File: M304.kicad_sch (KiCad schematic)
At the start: 89 parts, among them J1 LCD 2004, J2 Relay OUT, J3 iM920, J4 GPS, J5 Conn_01x02, P1 Digital, P10 CONN_01X01, P11 CONN_01X01, P12 CONN_01X01, P13 CONN_01X01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

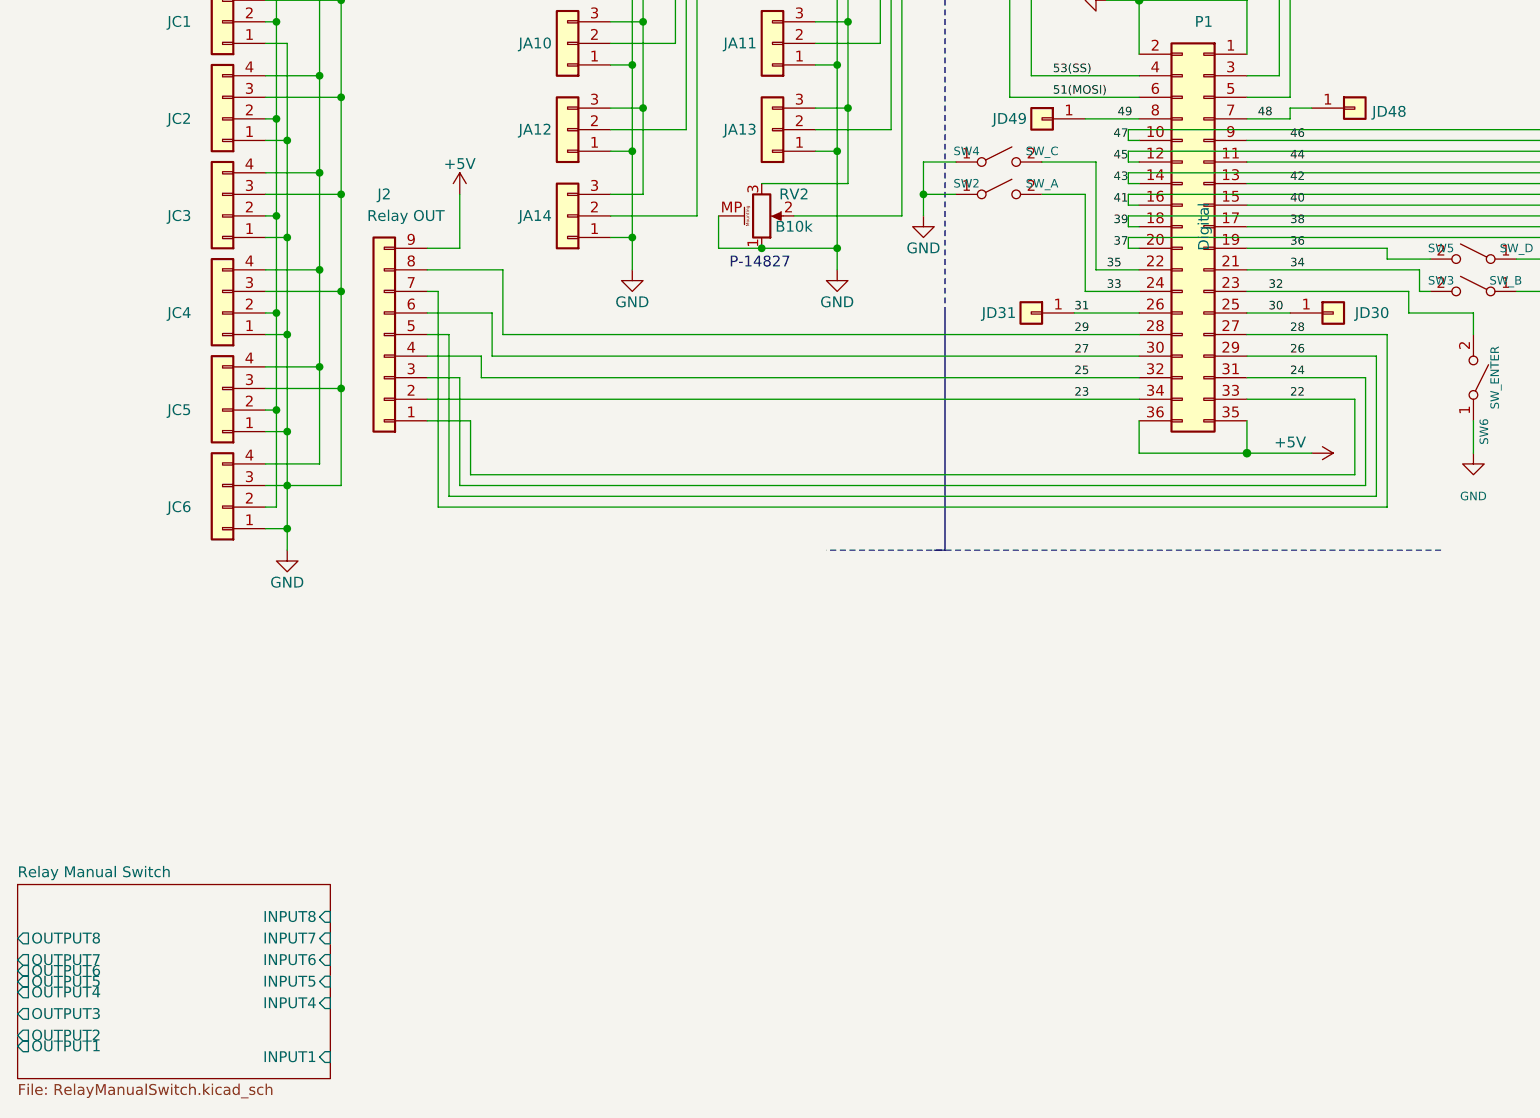
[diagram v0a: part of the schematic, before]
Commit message: RelayManualSwitch回路充実
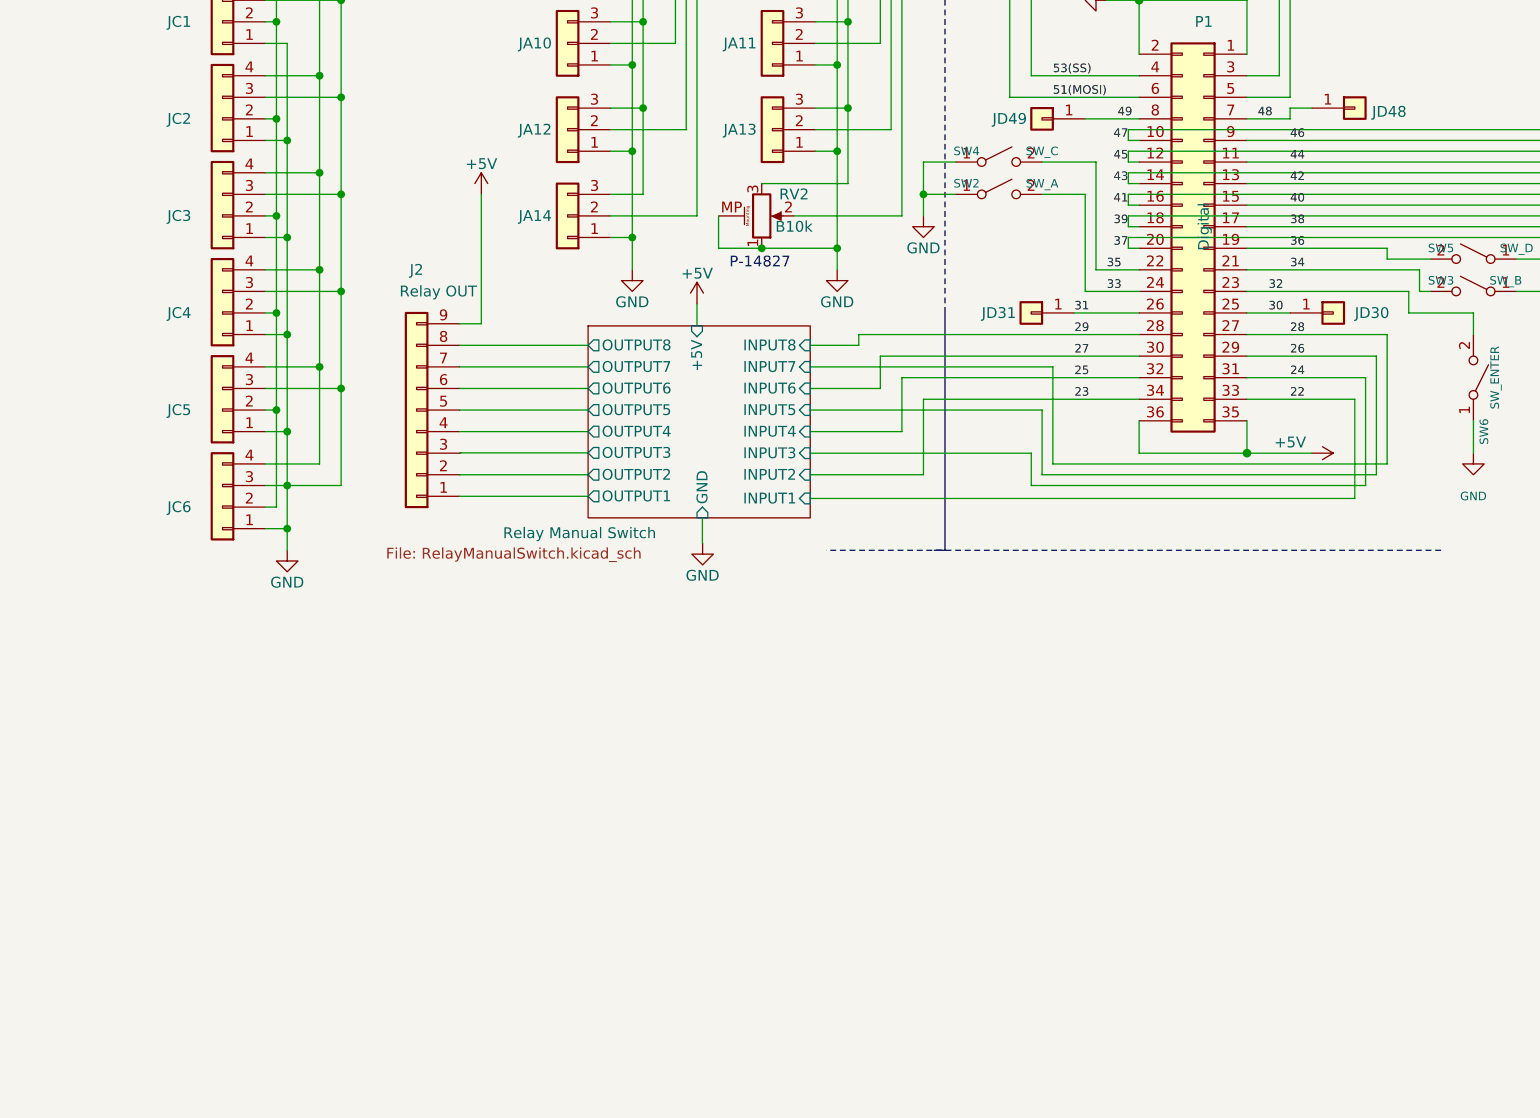
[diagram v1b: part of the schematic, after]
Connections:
- net 22: no longer J2.1 (Pin_1)
- net 23: no longer J2.2 (Pin_2)
- net 24: no longer J2.3 (Pin_3)
- net 25: no longer J2.4 (Pin_4)
- net 26: no longer J2.5 (Pin_5)
- net 27: no longer J2.6 (Pin_6)
- net 28: no longer J2.7 (Pin_7)
- net 29: no longer J2.8 (Pin_8)
- net Relay Manual Switch/OUTPUT1: now also J2.1 (Pin_1)
- net Relay Manual Switch/OUTPUT2: now also J2.2 (Pin_2)
- net Relay Manual Switch/OUTPUT3: now also J2.3 (Pin_3)
- net Relay Manual Switch/OUTPUT4: now also J2.4 (Pin_4)
- net Relay Manual Switch/OUTPUT5: now also J2.5 (Pin_5)
- net Relay Manual Switch/OUTPUT6: now also J2.6 (Pin_6)
- net Relay Manual Switch/OUTPUT7: now also J2.7 (Pin_7)
- net Relay Manual Switch/OUTPUT8: now also J2.8 (Pin_8)
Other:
- sheet Relay Manual Switch ports: added +5V, GND, INPUT2, INPUT3; removed none
- moved on the sheet: J2

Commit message: Mode STAT monitoring
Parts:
- removed JD31: Conn_01x01, Connector_Pin:Pin_D0.9mm_L10.0mm_W2.4mm_FlatFork, symbol Connector_Generic:Conn_01x01
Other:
- sheet Relay Manual Switch ports: added STAT; removed none
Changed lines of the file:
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@@
     (stroke (width 0) (type solid) (color 0 0 0 0))
   )
+  (wire (pts (xy 83.82 163.83) (xy 133.35 163.83))
+    (stroke (width 0) (type default) (color 0 0 0 0))
+  )
   (wire (pts (xy 252.73 30.48) (xy 255.27 30.48))
     (stroke (width 0) (type default) (color 0 0 0 0))
@@
     (stroke (width 0) (type default) (color 0 0 0 0))
   )
-  (wire (pts (xy 133.35 163.83) (xy 125.73 163.83))
-    (stroke (width 0) (type solid) (color 0 0 0 0))
-  )
   (wire (pts (xy 104.14 109.22) (xy 135.89 109.22))
     (stroke (width 0) (type default) (color 0 0 0 0))
@@
     (stroke (width 0) (type default) (color 0 0 0 0))
   )
+  (wire (pts (xy 83.82 163.83) (xy 83.82 165.354))
+    (stroke (width 0) (type default) (color 0 0 0 0))
+  )
   (wire (pts (xy 271.78 17.78) (xy 269.24 17.78))
     (stroke (width 0) (type default) (color 0 0 0 0))
@@
     (pin "2")
   )
-  (symbol (lib_id "Connector_Generic:Conn_01x01") (at 120.65 163.83 0) (mirror y) (unit 1)
-    (in_bom yes) (on_board yes)
-    (property "Reference" "JD31" (id 0) (at 116.84 163.83 0))
-    (property "Value" "Conn_01x01" (id 1) (at 120.65 161.3971 0)
-      (effects (font (size 1.27 1.27)) hide)
-    )
-    (property "Footprint" "Connector_Pin:Pin_D0.9mm_L10.0mm_W2.4mm_FlatFork" (id 2) (at 120.65 163.83 0)
-      (effects (font (size 1.27 1.27)) hide)
-    )
-    (property "Datasheet" "~" (id 3) (at 120.65 163.83 0)
-      (effects (font (size 1.27 1.27)) hide)
-    )
-    (pin "1")
-  )
   (symbol (lib_id "power:GND") (at 33.02 109.22 0) (unit 1)
     (in_bom yes) (on_board yes)
@@
       (effects (font (size 1.27 1.27)) (justify left))
     )
+    (pin "STAT" input (at 83.82 165.354 90)
+      (effects (font (size 1.27 1.27)) (justify right))
+    )
   )
   (sheet_instances
@@
     )
     (path "/923cf744-f246-4b99-9093-f86e5817e7a4/74b97936-4962-4d8c-8297-ea27e9c720cb"
-      (reference "#PWR?") (unit 1) (value "GND") (footprint "")
+      (reference "#PWR0158") (unit 1) (value "GND") (footprint "")
     )
     (path "/923cf744-f246-4b99-9093-f86e5817e7a4/8eecf7a6-ba02-4b56-86c1-4b6121624f36"
-      (reference "#PWR?") (unit 1) (value "GND") (footprint "")
+      (reference "#PWR0159") (unit 1) (value "GND") (footprint "")
     )
     (path "/7629fb6d-20db-4e52-aca9-1faafbccf85c"
@@
       (reference "D2-2") (unit 1) (value "LED") (footprint "")
     )
+    (path "/923cf744-f246-4b99-9093-f86e5817e7a4/47483762-d7d0-4c20-b380-6fbcea955810"
+      (reference "D2-3") (unit 1) (value "1N4148") (footprint "Diode_THT:D_DO-35_SOD27_P7.62mm_Horizontal")
+    )
     (path "/6f005a80-49e2-4014-971a-0fdebe1c3bed"
       (reference "D3") (unit 1) (value "1N4148") (footprint "Diode_THT:D_DO-35_SOD27_P7.62mm_Horizontal")
@@
       (reference "JD30") (unit 1) (value "Conn_01x01") (footprint "Connector_Pin:Pin_D0.9mm_L10.0mm_W2.4mm_FlatFork")
     )
-    (path "/c9444dbf-6a90-407d-8c6b-f91ec54f63d1"
-      (reference "JD31") (unit 1) (value "Conn_01x01") (footprint "Connector_Pin:Pin_D0.9mm_L10.0mm_W2.4mm_FlatFork")
-    )
     (path "/b0e37c59-828f-45f4-9524-3ceeeb2c5150"
       (reference "JD48") (unit 1) (value "Conn_01x01") (footprint "Connector_Pin:Pin_D0.9mm_L10.0mm_W2.4mm_FlatFork")
@@
       (reference "R2-2") (unit 1) (value "510") (footprint "")
     )
+    (path "/923cf744-f246-4b99-9093-f86e5817e7a4/aaa27b19-2b0f-459a-a227-24bc82c9e15a"
+      (reference "R2-3") (unit 1) (value "510") (footprint "")
+    )
     (path "/2447acfb-c168-4f85-b4d3-c3630454679c"

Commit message: PCB Design start
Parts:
- BT1: footprint (none) -> Akizuki:CH74-2032LF
- J5: value Conn_01x02 -> POWER IN
- RV1: footprint (none) -> Potentiometer_THT:Potentiometer_Runtron_RM-065_Vertical
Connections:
- net +3V3: now also JA0.3 (Pin_3), JA1.3 (Pin_3), JA2.3 (Pin_3), JA3.3 (Pin_3), JA4.3 (Pin_3), JA5.3 (Pin_3), JA6.3 (Pin_3), JA7.3 (Pin_3)
- net +5V: now also C2.2; no longer C2.1, JA0.3 (Pin_3), JA1.3 (Pin_3), JA2.3 (Pin_3), JA3.3 (Pin_3), JA4.3 (Pin_3), JA5.3 (Pin_3), JA6.3 (Pin_3), JA7.3 (Pin_3)
- net GND: now also C2.1; no longer C2.2, JC1.3 (Pin_3), JC2.3 (Pin_3), JC3.3 (Pin_3), JC4.3 (Pin_3), JC5.3 (Pin_3), JC6.3 (Pin_3), P5.2 (Pin_2), R2.2, U1.5 (SDA), U2.5 (SDA)
- net at U1.1 (X1): now also Y1.1; no longer Y1.2
- net at U1.2 (X2): now also Y1.2 (1); no longer Y1.1
- new net SDA: JC1.3 (Pin_3), JC2.3 (Pin_3), JC3.3 (Pin_3), JC4.3 (Pin_3), JC5.3 (Pin_3), JC6.3 (Pin_3), P5.2 (Pin_2), R2.2, U1.5 (SDA), U2.5 (SDA)
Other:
- note added: "P-01443"
- note removed: "P-00706"
- moved on the sheet: C2, Y1

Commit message: PCB Design cont.
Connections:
- net +5V: now also R1.2; no longer R1.1
- net Reset: now also R1.1; no longer R1.2
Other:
- moved on the sheet: R1
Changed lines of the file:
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@@
     (pin "1")
   )
-  (symbol (lib_id "Device:R_US") (at 101.6 38.1 0) (unit 1)
+  (symbol (lib_id "Device:R_US") (at 101.6 38.1 180) (unit 1)
     (in_bom yes) (on_board yes) (fields_autoplaced)
     (property "Reference" "R1" (id 0) (at 103.251 37.2653 0)
-      (effects (font (size 1.27 1.27)) (justify left))
+      (effects (font (size 1.27 1.27)) (justify right))
     )
     (property "Value" "10k" (id 1) (at 103.251 39.8022 0)
-      (effects (font (size 1.27 1.27)) (justify left))
+      (effects (font (size 1.27 1.27)) (justify right))
     )
-    (property "Footprint" "Resistor_THT:R_Axial_DIN0207_L6.3mm_D2.5mm_P7.62mm_Horizontal" (id 2) (at 102.616 38.354 90)
+    (property "Footprint" "Resistor_THT:R_Axial_DIN0207_L6.3mm_D2.5mm_P7.62mm_Horizontal" (id 2) (at 100.584 37.846 90)
       (effects (font (size 1.27 1.27)) hide)
     )

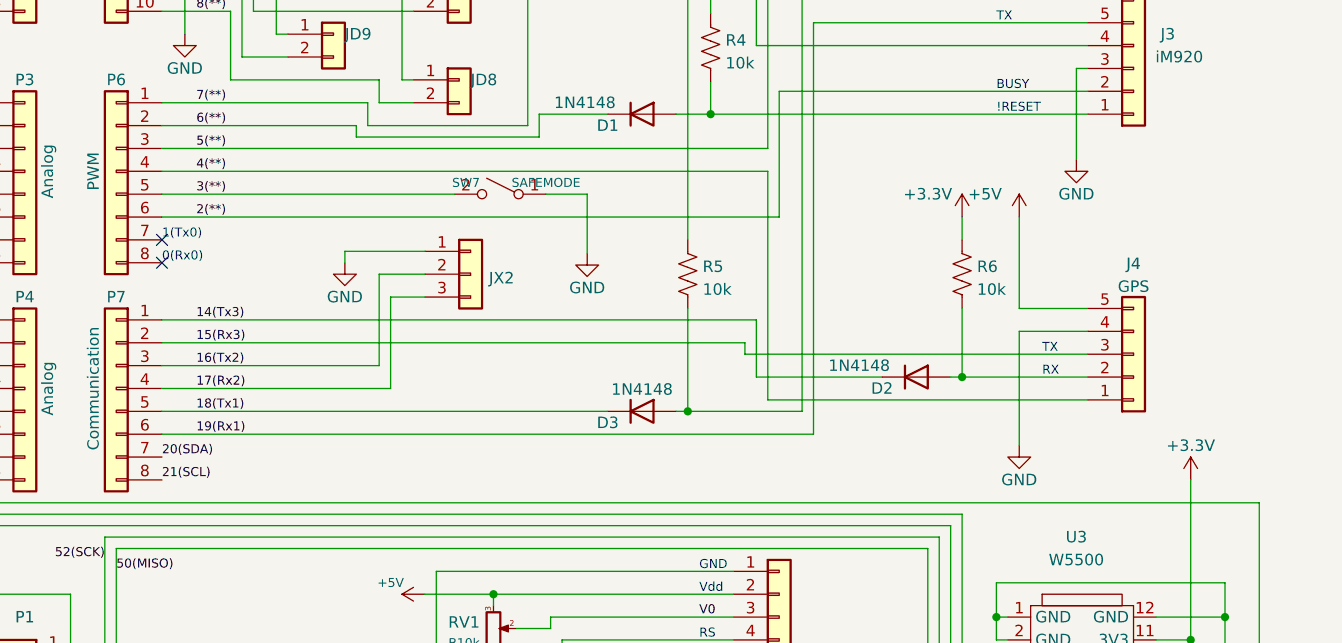
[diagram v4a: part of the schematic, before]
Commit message: UECS/MANUAL 切り替え表示LED
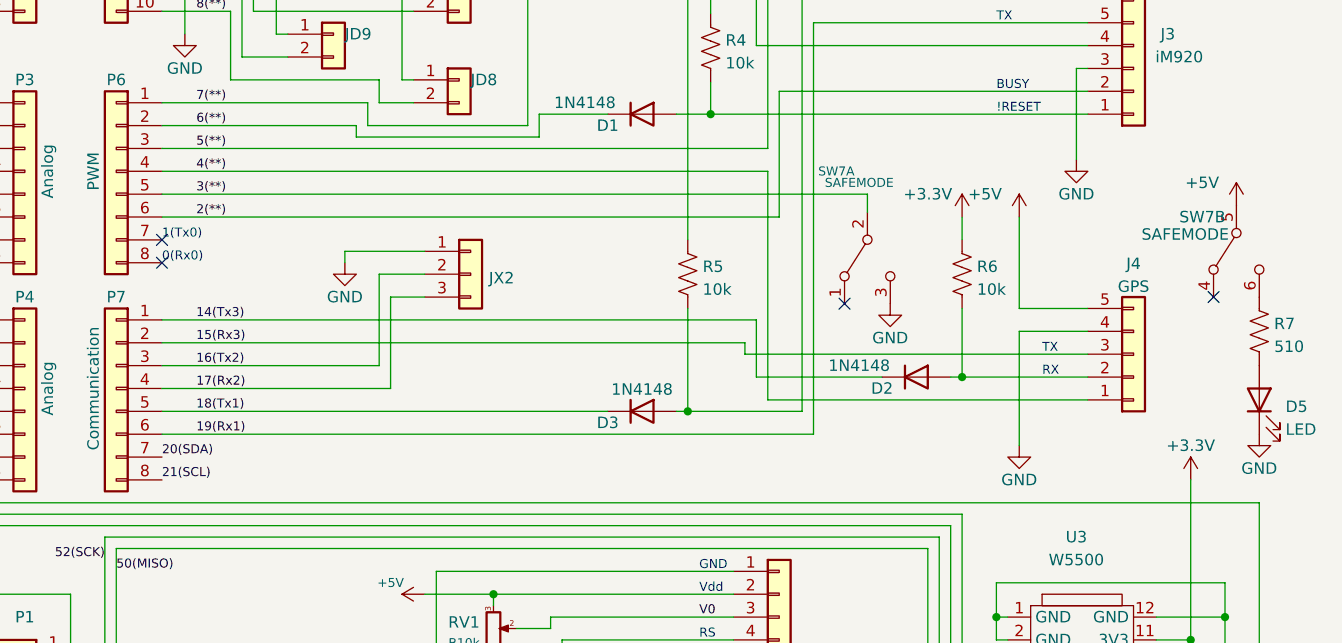
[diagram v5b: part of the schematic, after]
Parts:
- added D5: LED, LED_THT:LED_D3.0mm, symbol Device:LED
- added R7: 510, Resistor_THT:R_Axial_DIN0207_L6.3mm_D2.5mm_P7.62mm_Horizontal, symbol Device:R_US
- added unit 2 of SW7
- SW7: footprint (none) -> Akizuki:2MD1T2B4M2QNS; symbol Switch:SW_SPST -> Switch:SW_DPDT_x2
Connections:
- net +5V: now also SW7.5 (B)
- net GND: now also D5.1 (K); no longer SW7.1 (A)
- new net: D5.2 (A), R7.2
- new net: R7.1, SW7.6 (C)
- no-connect marks 10 -> 12

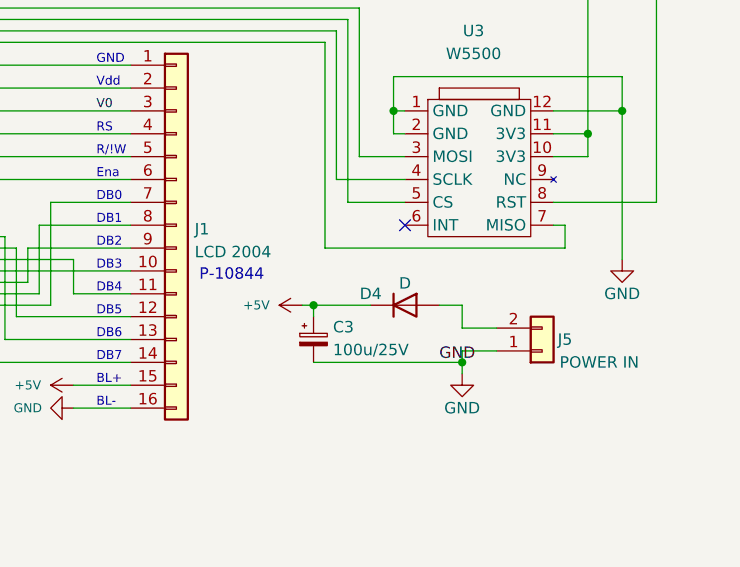
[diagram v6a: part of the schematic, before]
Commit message: 部品リストにAKICODEを追加した
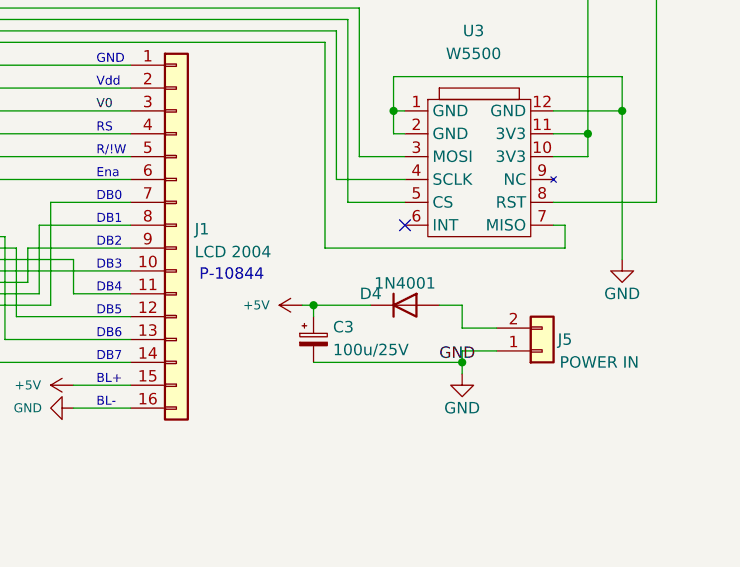
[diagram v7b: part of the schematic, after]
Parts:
- BT1: AKICODE (none) -> P-01443
- D4: value D -> 1N4001
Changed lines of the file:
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@@
+      (effects (font (size 1.27 1.27)) hide)
+    )
+    (property "AKICODE" "P-01443" (id 4) (at 26.67 46.99 0)
       (effects (font (size 1.27 1.27)) hide)
     )
@@
     (in_bom yes) (on_board yes)
     (property "Reference" "D4" (id 0) (at 246.38 149.86 0))
-    (property "Value" "D" (id 1) (at 250.19 148.6971 0))
+    (property "Value" "1N4001" (id 1) (at 250.19 148.6971 0))
     (property "Footprint" "Diode_THT:D_DO-35_SOD27_P10.16mm_Horizontal" (id 2) (at 250.19 151.13 0)
       (effects (font (size 1.27 1.27)) hide)
@@
     )
     (path "/c6d5e630-582e-45a8-9516-8a236c7c1136"
-      (reference "D4") (unit 1) (value "D") (footprint "Diode_THT:D_DO-35_SOD27_P10.16mm_Horizontal")
+      (reference "D4") (unit 1) (value "1N4001") (footprint "Diode_THT:D_DO-35_SOD27_P10.16mm_Horizontal")
     )
     (path "/2e92406e-50cb-44d6-a8bd-3dc4655ffc07"

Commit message: parts list 更新
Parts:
- C1, C2: AKICODE (none) -> P-17292
- C3: AKICODE (none) -> P-03123
- D1, D2, D3: AKICODE (none) -> I-00743
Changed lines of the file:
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@@
+      (effects (font (size 1.27 1.27)) hide)
+    )
+    (property "AKICODE" "I-00743" (id 4) (at 209.55 73.66 0)
       (effects (font (size 1.27 1.27)) hide)
     )
@@
       (effects (font (size 1.27 1.27)) hide)
     )
+    (property "AKICODE" "I-00743" (id 4) (at 209.55 106.68 0)
+      (effects (font (size 1.27 1.27)) hide)
+    )
     (pin "1")
     (pin "2")
@@
       (effects (font (size 1.27 1.27)) hide)
     )
-    (property "Datasheet" "~" (id 3) (at 68.58 33.02 0)
+    (property "Datasheet" "https://akizukidenshi.com/download/ds/murata/RDER71H104K0P1H03B.pdf" (id 3) (at 68.58 33.02 0)
+      (effects (font (size 1.27 1.27)) hide)
+    )
+    (property "AKICODE" "P-17292" (id 4) (at 68.58 33.02 0)
       (effects (font (size 1.27 1.27)) hide)
     )
@@
       (effects (font (size 1.27 1.27)) hide)
     )
-    (property "Datasheet" "~" (id 3) (at 241.3 29.21 0)
+    (property "Datasheet" "https://akizukidenshi.com/download/ds/murata/RDER71H104K0P1H03B.pdf" (id 3) (at 241.3 29.21 0)
+      (effects (font (size 1.27 1.27)) hide)
+    )
+    (property "AKICODE" "P-17292" (id 4) (at 241.3 29.21 0)
       (effects (font (size 1.27 1.27)) hide)
     )
@@
     )
     (property "Datasheet" "https://assets.nexperia.com/documents/data-sheet/1N4148_1N4448.pdf" (id 3) (at 240.03 102.87 0)
+      (effects (font (size 1.27 1.27)) hide)
+    )
+    (property "AKICODE" "I-00743" (id 4) (at 240.03 102.87 0)
       (effects (font (size 1.27 1.27)) hide)
     )
@@
       (effects (font (size 1.27 1.27)) hide)
     )
-    (property "Datasheet" "~" (id 3) (at 240.03 154.94 0)
-      (effects (font (size 1.27 1.27)) hide)
-    )
+    (property "Datasheet" "https://akizukidenshi.com/download/ds/rubycon/PK_series.pdf" (id 3) (at 240.03 154.94 0)
+      (effects (font (size 1.27 1.27)) hide)
+    )
+    (property "AKICODE" "P-03123" (id 4) (at 240.03 154.94 0)
+      (effects (font (size 1.27 1.27)) hide)
+    )
